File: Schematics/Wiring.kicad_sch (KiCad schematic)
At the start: 1 part, among them P1 USB_C_Plug_USB2.0

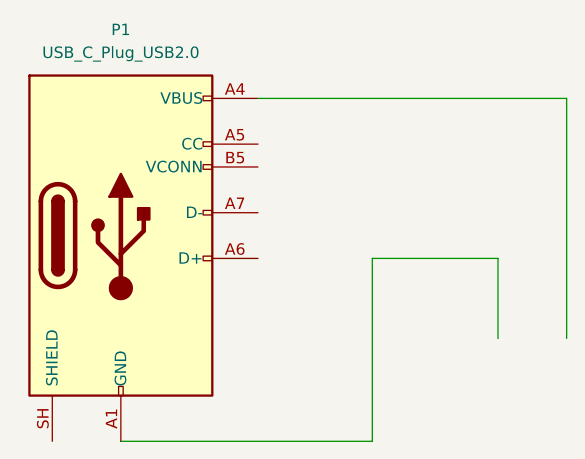
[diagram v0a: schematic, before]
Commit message: update wiring schematic
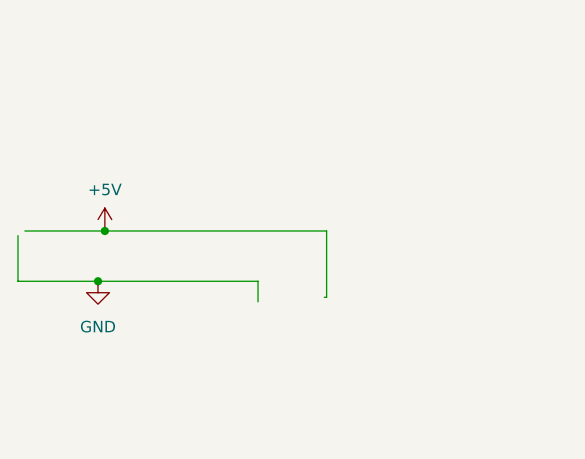
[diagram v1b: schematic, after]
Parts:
- removed P1: USB_C_Plug_USB2.0, symbol Connector:USB_C_Plug_USB2.0
